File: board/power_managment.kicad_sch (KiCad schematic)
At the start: 24 parts, among them J3 Bat IN Terminal, J4 Bat OUT Terminal, Q1 PMOS, U1 INA226, U3 AMS1117-3.3, U3 INA226, U4 LM2596S-5

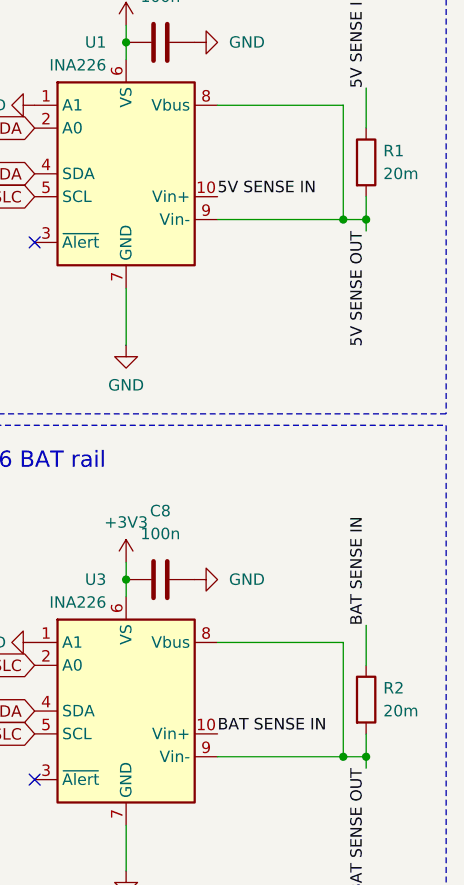
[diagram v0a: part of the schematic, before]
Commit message: Changed example of drone configuration, badly added option to set shunt value
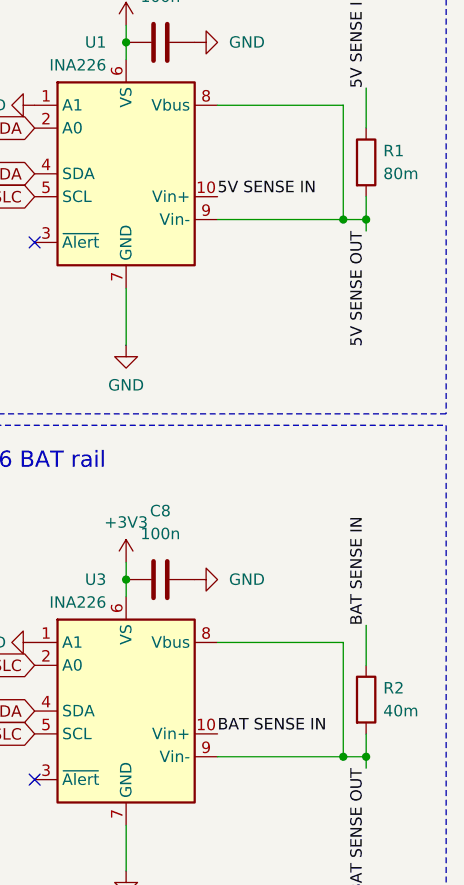
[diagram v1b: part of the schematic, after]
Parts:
- R1: value 20m -> 80m
- R2: value 20m -> 40m
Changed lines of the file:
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@@
       (effects (font (size 1.27 1.27)) (justify left))
     )
-    (property "Value" "20m" (at 273.05 50.165 0)
+    (property "Value" "80m" (at 273.05 50.165 0)
       (effects (font (size 1.27 1.27)) (justify left))
     )
@@
       (effects (font (size 1.27 1.27)) (justify left))
     )
-    (property "Value" "20m" (at 273.05 109.855 0)
+    (property "Value" "40m" (at 273.05 109.855 0)
       (effects (font (size 1.27 1.27)) (justify left))
     )
